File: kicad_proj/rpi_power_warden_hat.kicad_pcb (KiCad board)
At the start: 4 copper layers, 65 x 56.5 mm, 68 parts, among them J1 54-00164, J2 54-00164, J3 54-00003, J4 Raspberry Pi SMT connector, Q1 DMG2305UX-7, Q2 DMG2305UX-7, U1 INA260, U10 SN74AHC1G08DBVR, U2 INA260, U3 CAT24C32WI-GT3, U4 TPS563200, U5 DMMT5401-7-F, U6 TPS563200, U7 DMMT5401-7-F, U8 TPS22810DBVR, U9 SN74AHC1G08DBVR

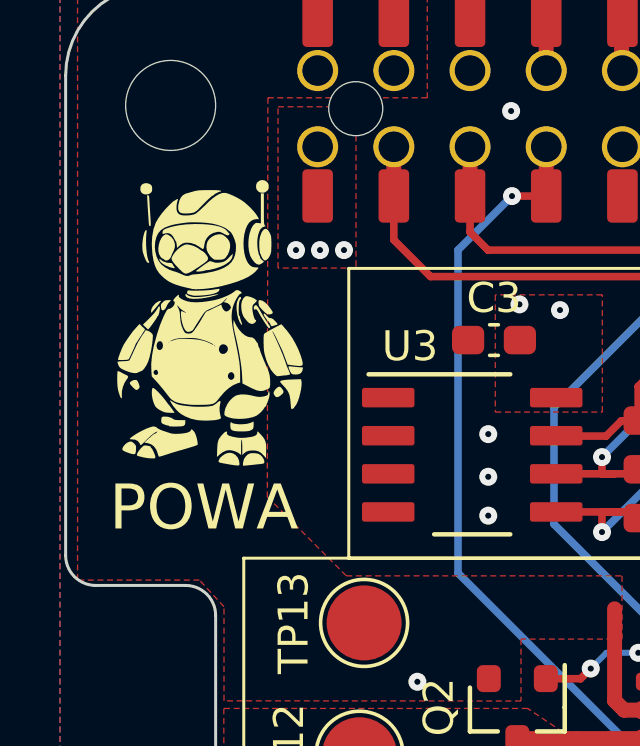
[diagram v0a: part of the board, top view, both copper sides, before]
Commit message: fix: DRCs due to logo
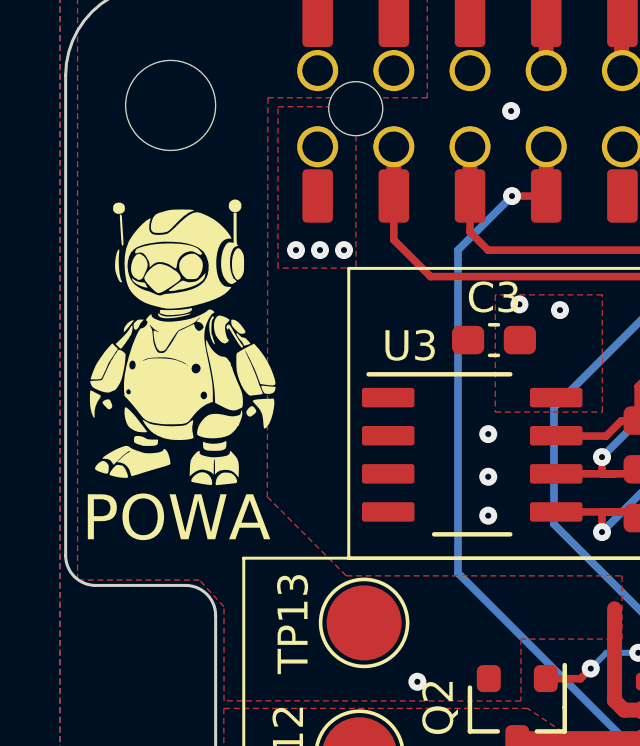
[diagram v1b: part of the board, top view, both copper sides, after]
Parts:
- moved G*** 1.12 mm to (130.6, 81.7)
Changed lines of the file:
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@@
 	(footprint "rpi_power_warden_hat:powa_logo"
 		(layer "F.Cu")
-		(at 131.503331 81.026635)
+		(at 130.593679 81.674121)
 		(property "Reference" "G***"
-			(at 0 0 0)
+			(at -0.01 -5.69 0)
 			(layer "F.SilkS")
 			(hide yes)
@@
 		)
 		(property "Value" "POWA"
-			(at 0 6.1976 0)
+			(at -0.01 5.91 0)
 			(layer "F.SilkS")
 			(effects
@@
 			(layer "F.SilkS")
 		)
+		(fp_rect
+			(start -3.16 -4.88)
+			(end 3.61 6.91)
+			(stroke
+				(width 0.05)
+				(type default)
+			)
+			(fill none)
+			(layer "F.CrtYd")
+		)
 	)

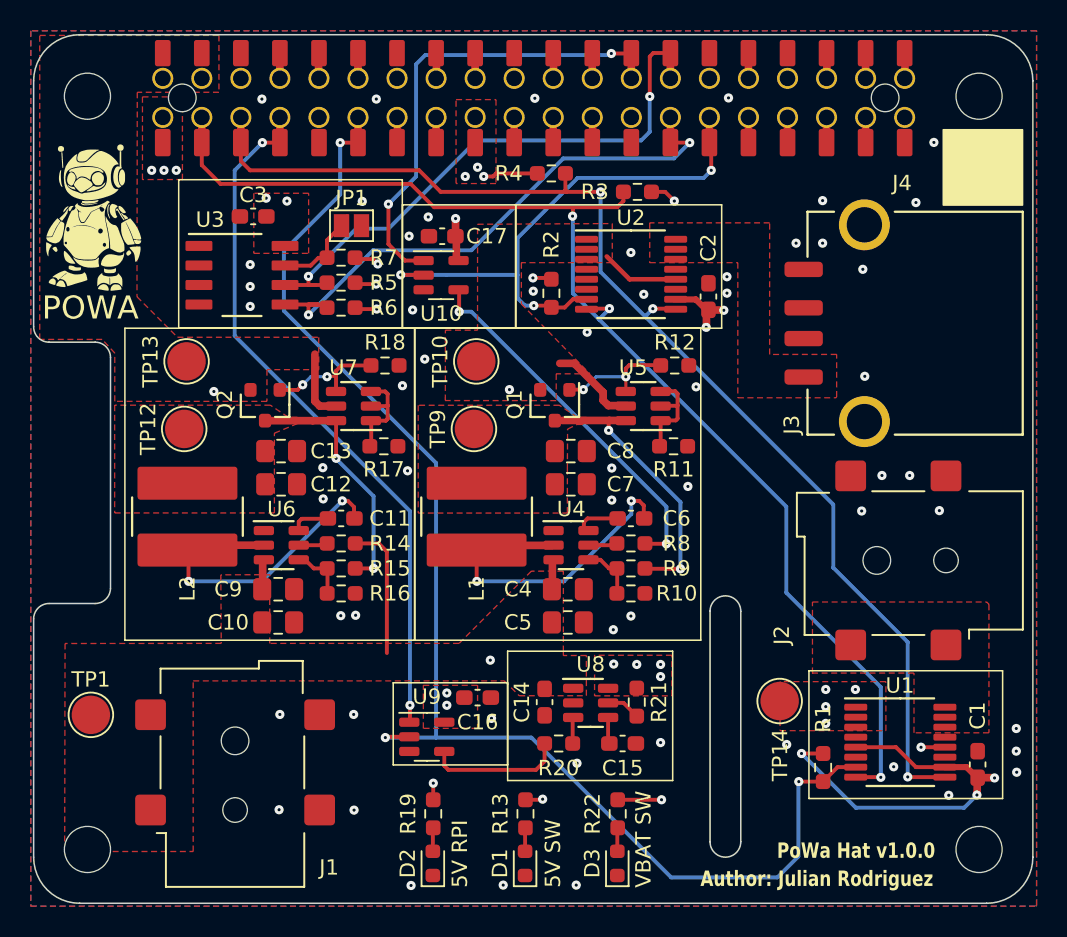
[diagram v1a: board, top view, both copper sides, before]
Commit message: add teardrops
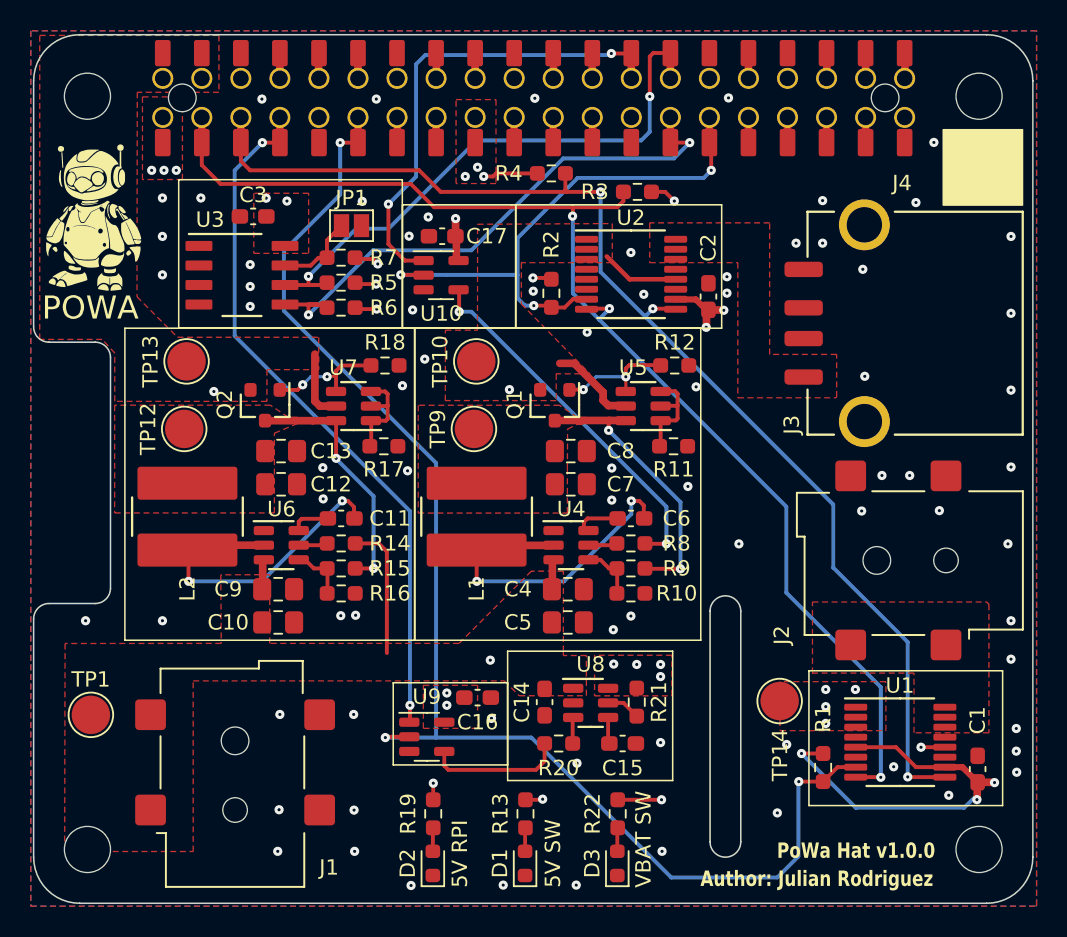
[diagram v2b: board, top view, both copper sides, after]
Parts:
- moved C1 0.30 mm to (188.3, 117.6)
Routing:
- net GND: vias 58 -> 76
